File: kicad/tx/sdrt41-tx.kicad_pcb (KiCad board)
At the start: 4 copper layers, 56 x 70.1 mm, 84 parts, among them J1 I, J2 Q, J3 Conn_01x05_Male, J4 TX, J5 Clock, J6 12V, Q1 2N3904_SOT23, T1 Transformer_1P_SS, U1 LM1117-3.3, U2 MC33078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

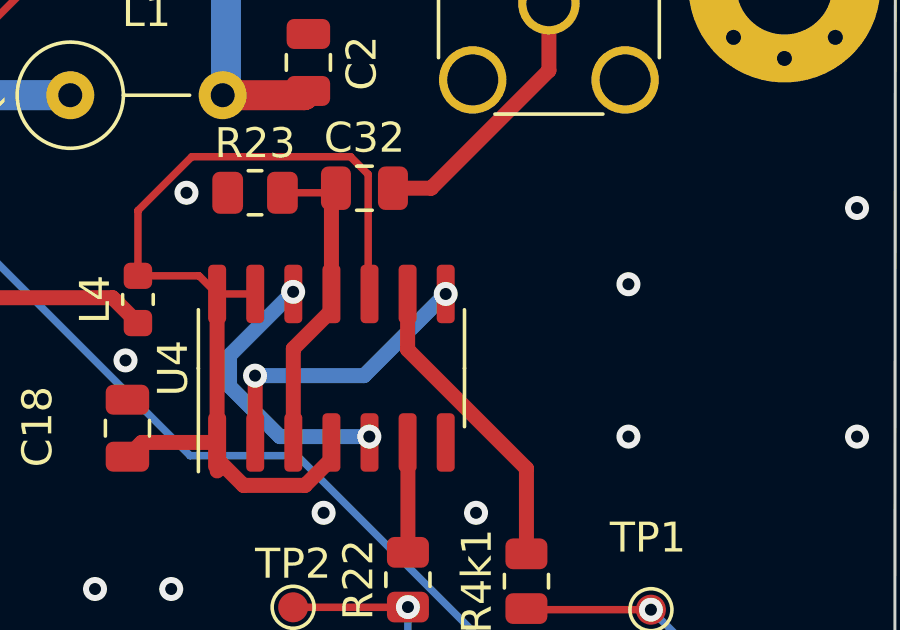
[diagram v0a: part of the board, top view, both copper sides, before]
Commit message: Update TX capacitors
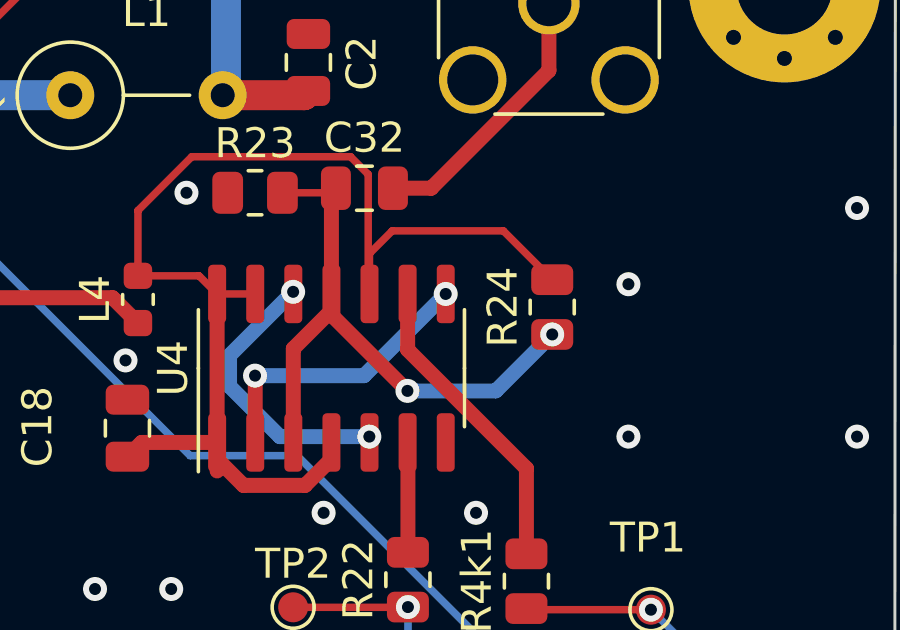
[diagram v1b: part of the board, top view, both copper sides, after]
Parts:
- added R24: 10k, Resistor_SMD:R_0805_2012Metric, F.Cu at (124.5, 64.3)
- C23, C24, C25, C26: value 2n2 -> 47n
- R23: value 50 -> 10k
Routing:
- net Net-(C32-Pad1): track 10.9 -> 20.8 mm, vias 0 -> 2
- net +3.3VP: track 33.7 -> 42.2 mm

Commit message: update gain and added differential  input setting
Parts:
- removed C32: 100n, Capacitor_SMD:C_0805_2012Metric
- removed R4k1: 4k7, Resistor_SMD:R_0805_2012Metric
- removed U1: LM1117-3.3, Package_TO_SOT_SMD:SOT-223-3_TabPin2
- added C35: 100p, Capacitor_SMD:C_0805_2012Metric, F.Cu at (120.0, 93.8)
- added C36: 100p, Capacitor_SMD:C_0805_2012Metric, F.Cu at (110.2, 84.3)
- C11: value 100u -> 100n; footprint Capacitor_THT:C_Radial_D5.0mm_H7.0mm_P2.00mm -> Capacitor_SMD:C_0805_2012Metric
- C23, C24, C25, C26: value 47n -> 2n2
- J5: value Clock -> TX
- R23: value 10k -> 4k7
- R24: value 10k -> 100
- moved C8 30.0 mm to (123.3, 60.8)
- moved C11 23.5 mm to (125.3, 63.4), turned to 180 degrees
- moved C26 17.4 mm to (130.7, 96.1), turned to 90 degrees
- moved R22 12.5 mm to (119.3, 60.8), turned to 0 degrees
- moved TP1 11.8 mm to (116.0, 73.8)
- moved C25 8.78 mm to (126.4, 85.1), turned to -90 degrees
- moved C23 8.40 mm to (133.2, 96.1), turned to 90 degrees
- moved TP2 8.14 mm to (124.0, 73.8)
- moved C20 5.59 mm to (115.2, 80.4)
- moved R24 4.66 mm to (129.0, 63.4), turned to 180 degrees
- moved L4 1.93 mm to (110.4, 62.1), turned to -90 degrees
- moved C24 1.43 mm to (122.9, 85.1), turned to -90 degrees
- moved J5 1.16 mm to (123.2, 54.1)
- moved R23 0.85 mm to (115.3, 60.8)
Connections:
- C11 pad 1: +3V3 -> Net-(C11-Pad1)
- C11 pad 2: GND -> Net-(U4-Pad11)
- C18 pad 2: +3.3VP -> V5P
- C8 pad 1: GND -> Net-(C8-Pad1)
- C8 pad 2: +3V3 -> Net-(U4-Pad11)
- J3 pad 1: unconnected-(J3-Pad1) -> GND
- J3 pad 2: unconnected-(J3-Pad2) -> GND
- J5 pad 1: Net-(C32-Pad2) -> Net-(C8-Pad1)
- L4 pad 1: +3V3 -> +5V
- L4 pad 2: +3.3VP -> V5P
- L5 pad 1: +3V3 -> +5V
- R19 pad 2: +3V3 -> +5V
- R22 pad 1: Net-(R22-Pad1) -> GND
- R22 pad 2: Net-(R22-Pad2) -> Net-(U4-Pad11)
- R23 pad 1: GND -> V5P
- R23 pad 2: Net-(C32-Pad1) -> Net-(U4-Pad11)
- R24 pad 1: Net-(C32-Pad1) -> GND
- R24 pad 2: +3.3VP -> Net-(C11-Pad1)
- TP1 pad 1: Net-(R4k1-Pad1) -> Net-(TP1-Pad1)
- TP2 pad 1: Net-(R22-Pad1) -> Net-(TP2-Pad1)
- U4 pad 1: +3.3VP -> V5P
- U4 pad 10: +3.3VP -> V5P
- U4 pad 11: Net-(C32-Pad1) -> Net-(U4-Pad11)
- U4 pad 13: +3.3VP -> V5P
- U4 pad 14: +3.3VP -> V5P
- U4 pad 3: Net-(C32-Pad1) -> Net-(U4-Pad11)
- U4 pad 4: +3.3VP -> V5P
- U4 pad 6: Net-(R22-Pad2) -> Net-(TP1-Pad1)
- U4 pad 9: Net-(R4k1-Pad2) -> Net-(TP2-Pad1)
- U5 pad 14: Net-(R4k1-Pad1) -> Net-(TP2-Pad1)
- U5 pad 2: Net-(R22-Pad1) -> Net-(TP1-Pad1)
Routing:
- net +3.3VP: track 42.2 -> 0.00 mm
- net Net-(TP2-Pad1): track 0.00 -> 41.1 mm, vias 0 -> 2
- net V5P: track 0.00 -> 31.3 mm
- net Net-(TP1-Pad1): track 0.00 -> 29.9 mm, vias 0 -> 2
- net Net-(R22-Pad1): track 24.3 -> 0.00 mm, vias 2 -> 0
- net +3V3: track 24.0 -> 0.00 mm, vias 3 -> 0
- net Net-(R4k1-Pad1): track 22.1 -> 0.00 mm, vias 2 -> 0
- net Net-(C32-Pad1): track 20.8 -> 0.00 mm, vias 2 -> 0
- net Net-(U4-Pad11): track 0.00 -> 19.3 mm
- net Net-(R4k1-Pad2): track 10.3 -> 0.00 mm
- net Net-(C32-Pad2): track 9.05 -> 0.00 mm
- net +5V: track 99.9 -> 108.2 mm, vias 3 -> 5
- net Net-(C8-Pad1): track 0.00 -> 7.18 mm
- net Net-(C20-Pad2): track 10.4 -> 6.16 mm
- net Net-(C20-Pad1): track 6.48 -> 10.3 mm
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- added copper zone on In2.Cu, net +5V
- removed copper zone on In2.Cu, net +3V3
